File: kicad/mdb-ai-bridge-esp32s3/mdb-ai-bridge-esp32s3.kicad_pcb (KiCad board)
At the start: 2 copper layers, 60 x 37.9 mm, 94 parts, among them J3 Conn_02x08_Top_Bottom, J7 USB_C_Receptacle_USB2.0_16P, SW3 SW_Push, SW4 SW_Push, SW5 SW_Push, SW9 SW_Push, U10 ESP32-S3FH4R2, U11 ESP32-S3FH4R2, U12 ESP32-S3FH4R2, U13 AMS1117-3.3, U14 USB2514B_Bi, Y2 24MHz, Y3 40MHz, Y4 40MHz, Y5 40MHz

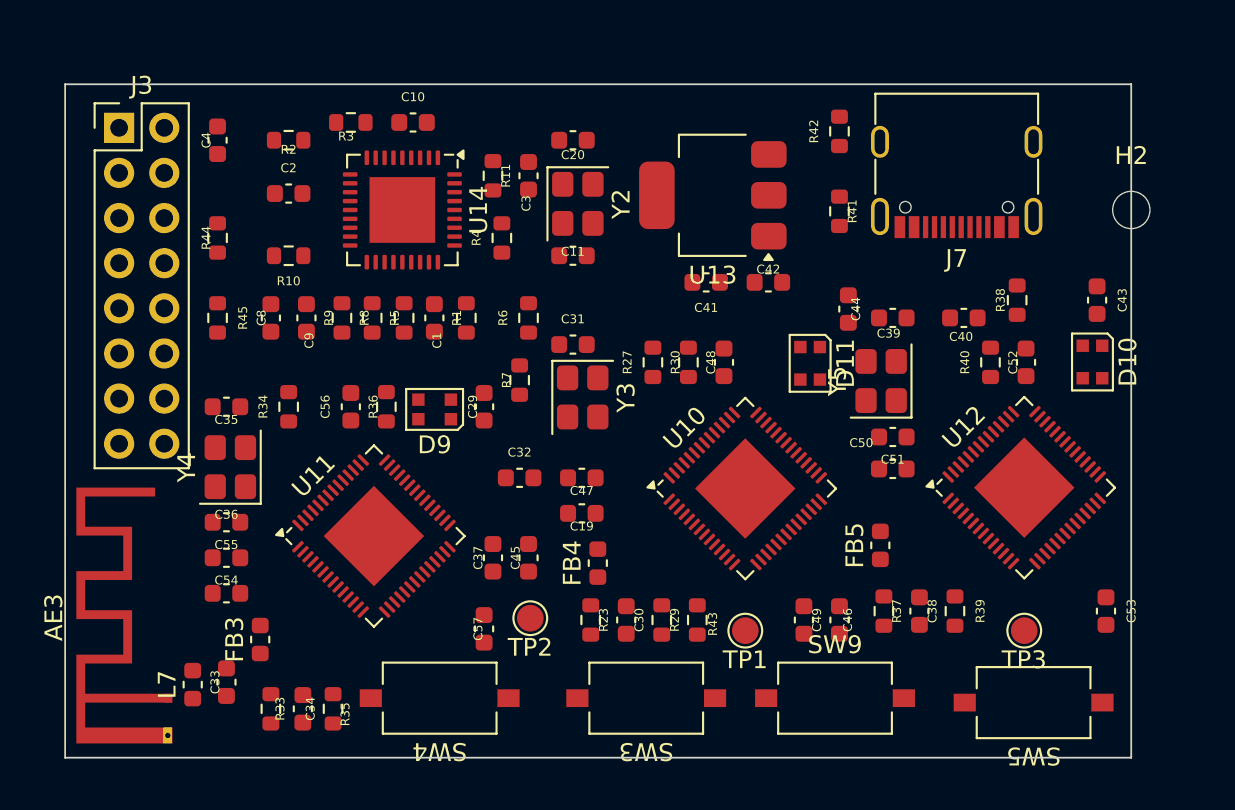
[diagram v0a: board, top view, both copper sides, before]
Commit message: Enlarge Edge.Cuts to 64x41mm and move H2 mounting hole to right edge
- Edge.Cuts was 58x37mm, too small for the 94 placed footprints
  (needed ~59.2x37.7mm); grew outline to (130,75)-(194,116) instead of
  compacting placement.
- H2 mounting hole moved to x=194 (board right edge) so its courtyard
  sits exactly 50% inside / 50% outside the board, per request.
- Validated with pcbnew (python): 0 footprints outside Edge.Cuts
  (except H2, intentionally straddling) and kicad-cli drc (176
  pre-existing violations unchanged, no new ones from this change).

Co-Authored-By: Claude Sonnet 5 <noreply@anthropic.com>
Claude-Session: https://claude.ai/code/session_0141XSaXvjY2LuYvwcHP9FdA
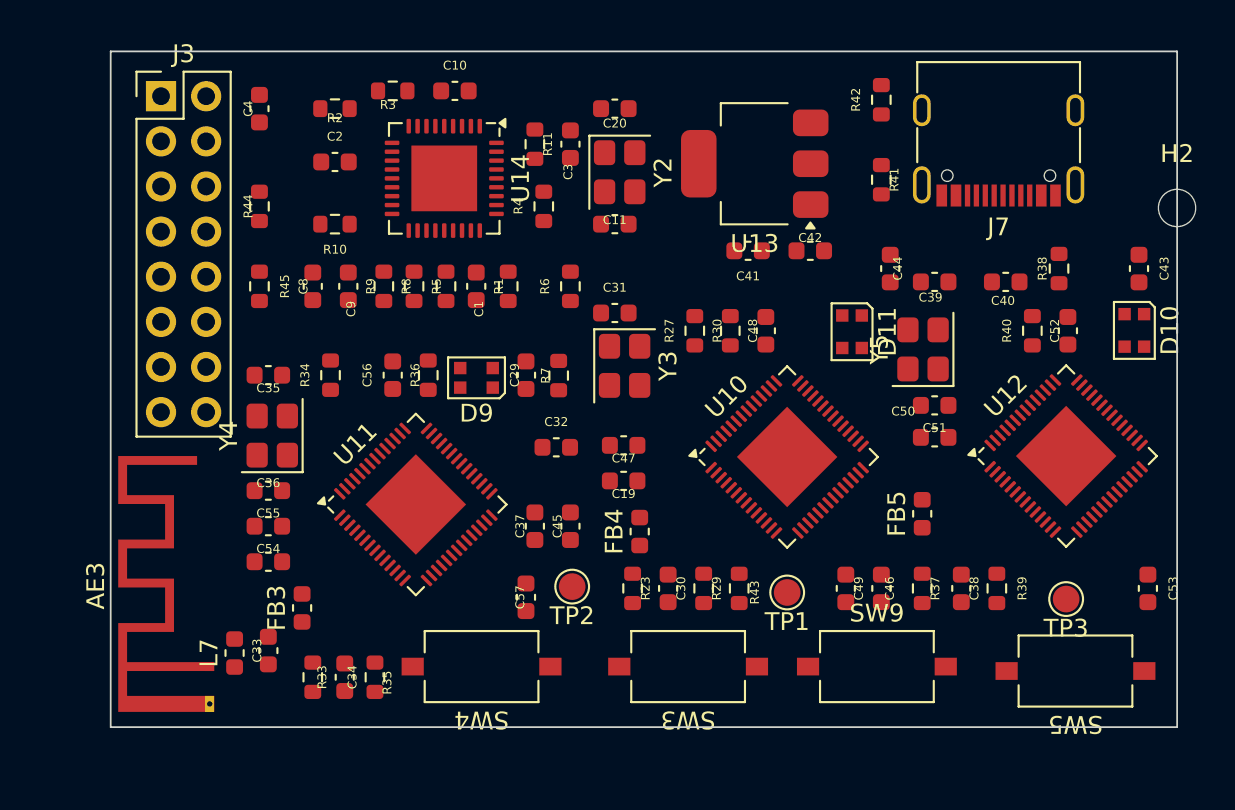
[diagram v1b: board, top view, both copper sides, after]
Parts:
- moved C44 3.28 mm to (177.9, 87.2)
- moved TP1 3.19 mm to (172.1, 105.5)
- moved C2 3.16 mm to (146.6, 81.2)
- moved R10 3.16 mm to (146.6, 84.7)
- moved R2 3.16 mm to (146.6, 78.2)
- moved C39 3.11 mm to (180.4, 88.0)
- moved C40 3.11 mm to (184.4, 88.0)
- moved C19 2.98 mm to (162.9, 99.2)
- moved C47 2.98 mm to (162.9, 97.2)
- moved C30 2.95 mm to (165.4, 105.2)
- moved AE3 2.95 mm to (139.6, 109.6)
- moved C1 2.95 mm to (154.6, 88.2)
- moved R8 2.95 mm to (151.1, 88.2)
- moved U12 2.95 mm to (187.8, 97.8)
- moved C10 2.95 mm to (153.4, 77.2)
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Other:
- board size 60 x 37.9 mm -> 60 x 38 mm
